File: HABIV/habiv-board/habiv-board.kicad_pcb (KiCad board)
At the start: 4 copper layers, 100.3 x 120.9 mm, 128 parts, among them IC1 RTC_PCF8523T, J1 Micro_SD_Card_Det, J10 Conn_01x02_Female, J11 Conn_01x02_Female, J12 Conn_01x02_Female, J13 Conn_01x02_Female, J14 Conn_01x02_Female, J15 Conn_01x02_Female, J16 Conn_01x02_Female, J17 Conn_01x03_Male, J18 Conn_01x03_Male, J19 Conn_01x03_Male, J2 Conn_ARM_JTAG_SWD_20, J20 Conn_01x05_Male, J21 Conn_01x04_Male, J3 Conn_01x02_Male, J4 Conn_01x16_Male, J5 Conn_01x03_Male, J6 Conn_01x16_Male, J7 Conn_01x16_Male, J8 Conn_01x02_Female, J9 Conn_01x02_Male, Q1 32.768KHz, SW1 SW_DPST_x2, U1 STM32F401RET6, U2 MAX31855, U3 FGPMMOPA6H, U4 TPS564208, U5 TPS564208, U6 LSM9DS1TR, U7 MS560702BA03-00, Y1 32.768MHz

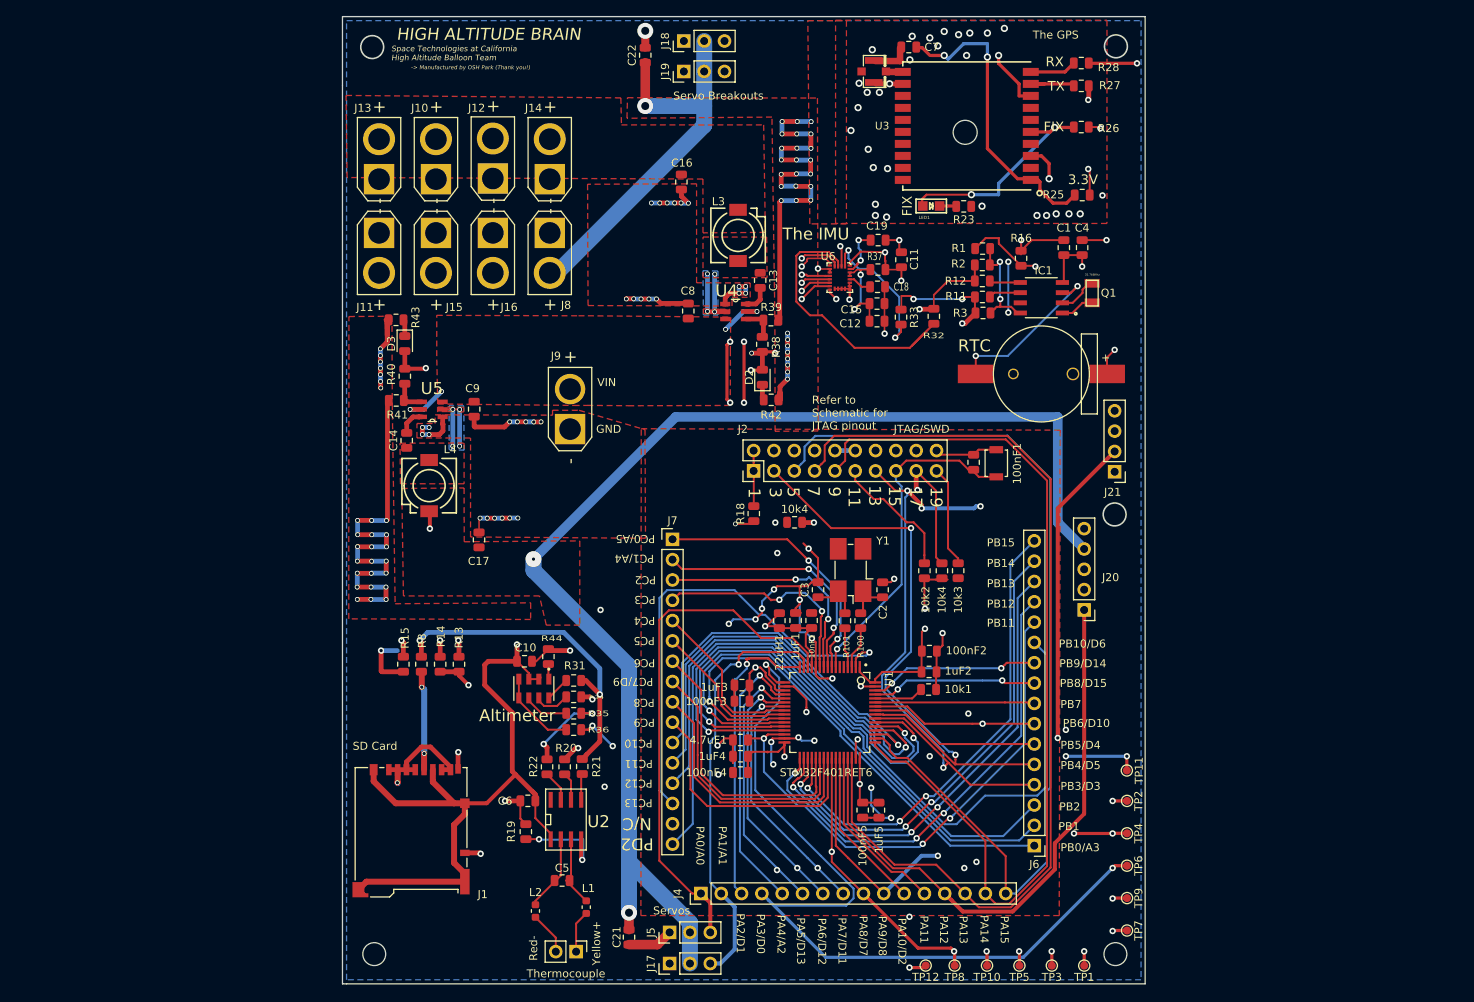
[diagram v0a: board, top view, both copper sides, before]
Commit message: Turned IMU into breakout pins, minor changes, unfinished!
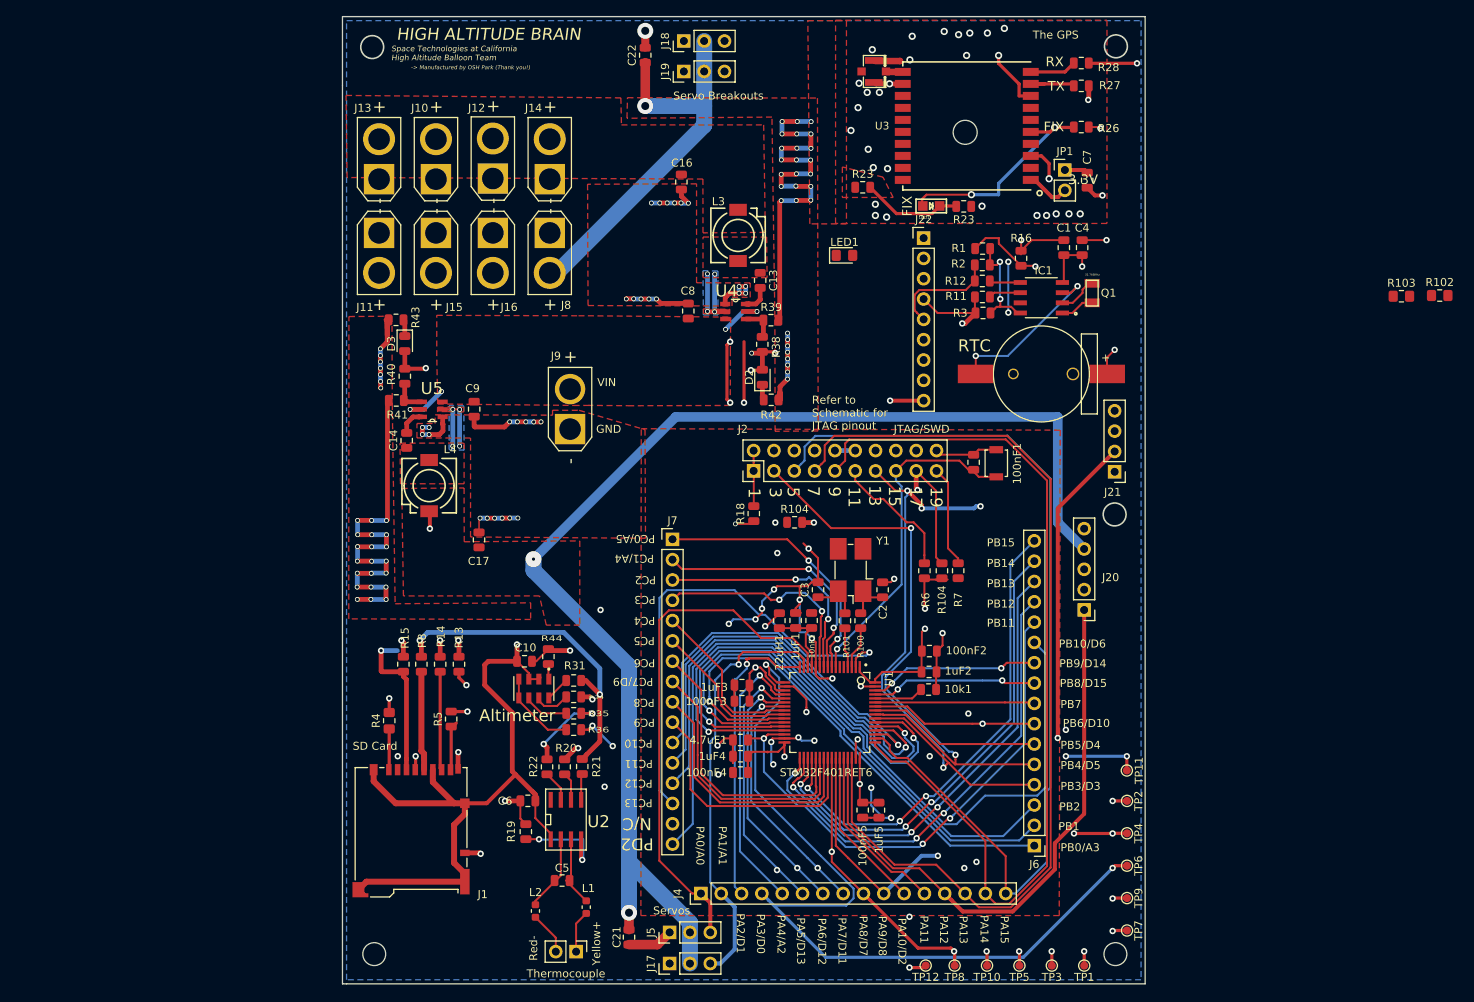
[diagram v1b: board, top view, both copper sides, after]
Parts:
- removed C11, C12, C19: 100n, Capacitor_SMD:C_0805_2012Metric
- removed C15: 10u, Capacitor_SMD:C_0805_2012Metric
- removed C18: 10n, Capacitor_SMD:C_0805_2012Metric
- removed R25, R32, R33, R37: 0, Resistor_SMD:R_0805_2012Metric
- removed U6: LSM9DS1TR, digikey-footprints:LGA-24_3x3.5mm_LSM9DS1
- added J22: Conn_01x09_Male, Connector_PinHeader_2.54mm:PinHeader_1x09_P2.54mm_Vertical, F.Cu at (153.7, 36.8)
- added JP1: Jumper, Connector_PinHeader_2.54mm:PinHeader_1x02_P2.54mm_Vertical, F.Cu at (171.3, 28.3)
- added LED1: RED, LED_SMD:LED_0805_2012Metric_Pad1.15x1.40mm_HandSolder, F.Cu at (143.8, 39.0)
- added R102: 10K, Resistor_SMD:R_0805_2012Metric_Pad1.15x1.40mm_HandSolder, F.Cu at (218.2, 44.0)
- added R103: 10K, Resistor_SMD:R_0805_2012Metric_Pad1.15x1.40mm_HandSolder, F.Cu at (213.4, 44.1)
- added R23: 1K, Resistor_SMD:R_0805_2012Metric, F.Cu at (146.1, 30.5)
- added R4: 0, Resistor_SMD:R_0805_2012Metric_Pad1.15x1.40mm_HandSolder, F.Cu at (86.9, 97.2)
- added R5: 0, Resistor_SMD:R_0805_2012Metric, F.Cu at (94.6, 96.9)
- R104 (x2): renamed from 10k4; value R8 -> 10K
- R6: renamed from 10k2; value R6 -> 10K
- R7: renamed from 10k3; value R7 -> 10K
- moved C7 27.8 mm to (174.1, 29.6), turned to 270 degrees
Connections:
- 10nF1 pad 2: +3V3 -> Net-(10nF1-Pad2)
- 1uF1 pad 2: +3V3 -> Net-(10nF1-Pad2)
- 22uH1 pad 1: +3V3 -> Net-(10nF1-Pad2)
- C7 pad 1: Net-(C7-Pad1) -> +3V3
- IC1 pad 7: (no net) -> Net-(IC1-Pad7)
- J1 pad 1: +3V3 -> Net-(J1-Pad1)
- J1 pad 2: +3V3 -> Net-(J1-Pad2)
- J1 pad 3: +3V3 -> Net-(J1-Pad3)
- J1 pad 7: +3V3 -> Net-(J1-Pad7)
- J1 pad 8: +3V3 -> Net-(J1-Pad8)
- J7 pad 15: (no net) -> Net-(J7-Pad15)
- R13 pad 2: +3V3 -> Net-(J1-Pad2)
- R14 pad 1: +3V3 -> Net-(J1-Pad7)
- R15 pad 2: +3V3 -> Net-(J1-Pad3)
- U1 pad 13: +3V3 -> Net-(10nF1-Pad2)
- U1 pad 5: (no net) -> Net-(U1-Pad5)
- U1 pad 6: (no net) -> Net-(U1-Pad6)
- U3 pad P$1: Net-(C7-Pad1) -> Net-(JP1-Pad2)
- U4 pad 5: Net-(C8-Pad1) -> Net-(R102-Pad1)
- U5 pad 5: Net-(C8-Pad1) -> Net-(R103-Pad1)
- Y1 pad 2: (no net) -> Net-(Y1-Pad2)
- Y1 pad 3: (no net) -> Net-(Y1-Pad3)
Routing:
- net PC3: track 82.1 -> 151.7 mm
- net +3V3: track 133.9 -> 81.8 mm, vias 21 -> 15
- net Net-(C7-Pad1): track 38.3 -> 0.00 mm, vias 2 -> 0
- net Net-(R32-Pad1): track 37.8 -> 0.00 mm
- net Net-(J1-Pad3): track 0.00 -> 19.8 mm, vias 0 -> 1
- net Net-(R33-Pad1): track 19.1 -> 0.00 mm, vias 2 -> 0
- net PC4: track 75.0 -> 59.7 mm, vias 3 -> 1
- net Net-(J1-Pad2): track 0.00 -> 14.6 mm, vias 0 -> 2
- net GND: track 424.3 -> 410.0 mm, vias 147 -> 142
- net Net-(C12-Pad1): track 12.9 -> 0.00 mm, vias 2 -> 0
- net Net-(C8-Pad1): track 12.7 -> 0.00 mm, vias 4 -> 0
- net Net-(J1-Pad7): track 0.00 -> 12.3 mm
- net PC2: track 76.6 -> 65.2 mm, vias 3 -> 2
- net PC6: track 94.4 -> 83.8 mm, vias 1 -> 0
- net Net-(LED1-PadC): track 2.08 -> 12.5 mm
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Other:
- net class Default: trace_width 0.4 -> 0.5
- board text removed: "The IMU"

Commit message: Changed IMU pinout, fixed some grounding issues
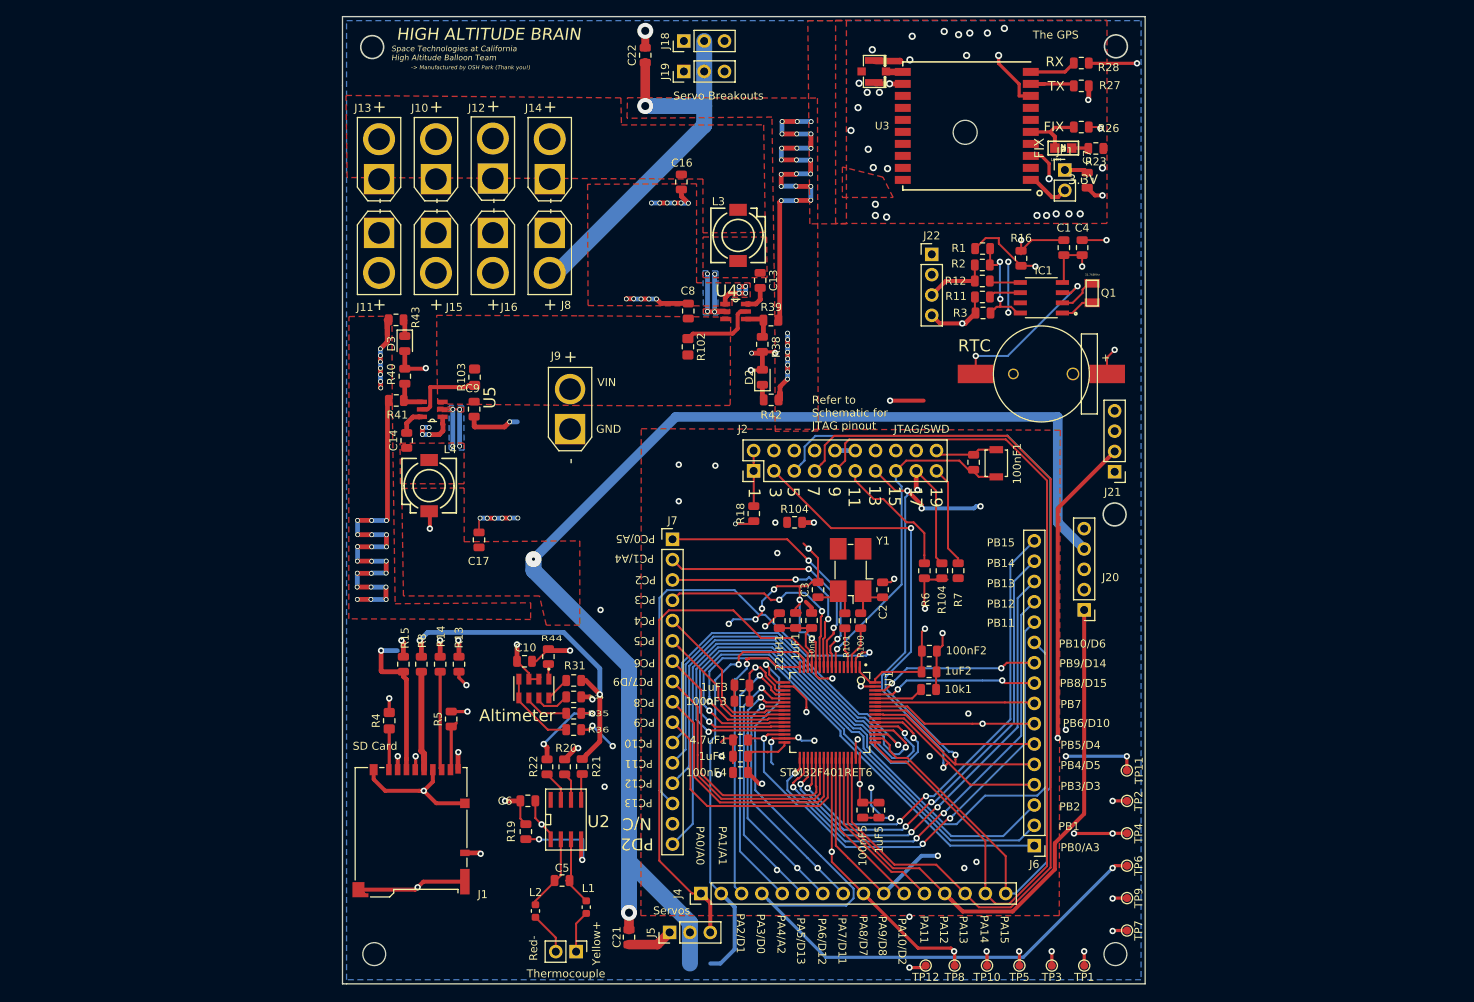
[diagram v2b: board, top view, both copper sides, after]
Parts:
- removed J17: Conn_01x03_Male, Connector_PinHeader_2.54mm:PinHeader_1x03_P2.54mm_Vertical
- removed the LED1 at (143.8, 39.0)
- removed the R23 at (146.1, 30.5)
- J22: value Conn_01x09_Male -> Conn_01x04_Male; footprint Connector_PinHeader_2.54mm:PinHeader_1x09_P2.54mm_Vertical -> Connector_PinHeader_2.54mm:PinHeader_1x04_P2.54mm_Vertical
- moved R103 116.3 mm to (97.5, 54.2), turned to 90 degrees
- moved R102 94.2 mm to (124.2, 50.4), turned to 270 degrees
- moved R23 18.0 mm to (175.2, 25.6)
- moved LED1 18.0 mm to (171.1, 25.6)
- moved J22 2.27 mm to (154.7, 38.9)
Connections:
- J22 pad 1: +3V3 -> GND
- J22 pad 2: Net-(J22-Pad2) -> +3V3
- J22 pad 3: GND -> PB9
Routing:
- net GND: track 410.0 -> 363.8 mm, vias 142 -> 143
- net PC4: track 59.7 -> 21.1 mm, vias 1 -> 0
- net Net-(LED1-PadA): track 27.9 -> 7.90 mm, vias 2 -> 0
- net Net-(LED1-PadC): track 12.5 -> 2.08 mm
- net PB9: track 109.7 -> 103.6 mm
- net Net-(R102-Pad1): track 6.33 -> 9.70 mm, vias 2 -> 0
- net PB8: track 121.7 -> 118.7 mm
- net Net-(R103-Pad1): track 6.33 -> 9.25 mm, vias 2 -> 0
- net Net-(J1-Pad2): track 14.6 -> 16.3 mm
- net PC7: track 125.3 -> 126.2 mm
- net +3V3: track 81.8 -> 82.4 mm
- net PC3: track 151.7 -> 151.3 mm, vias 5 -> 3

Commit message: Moved RockBlock Connector, removed some Servo breakouts
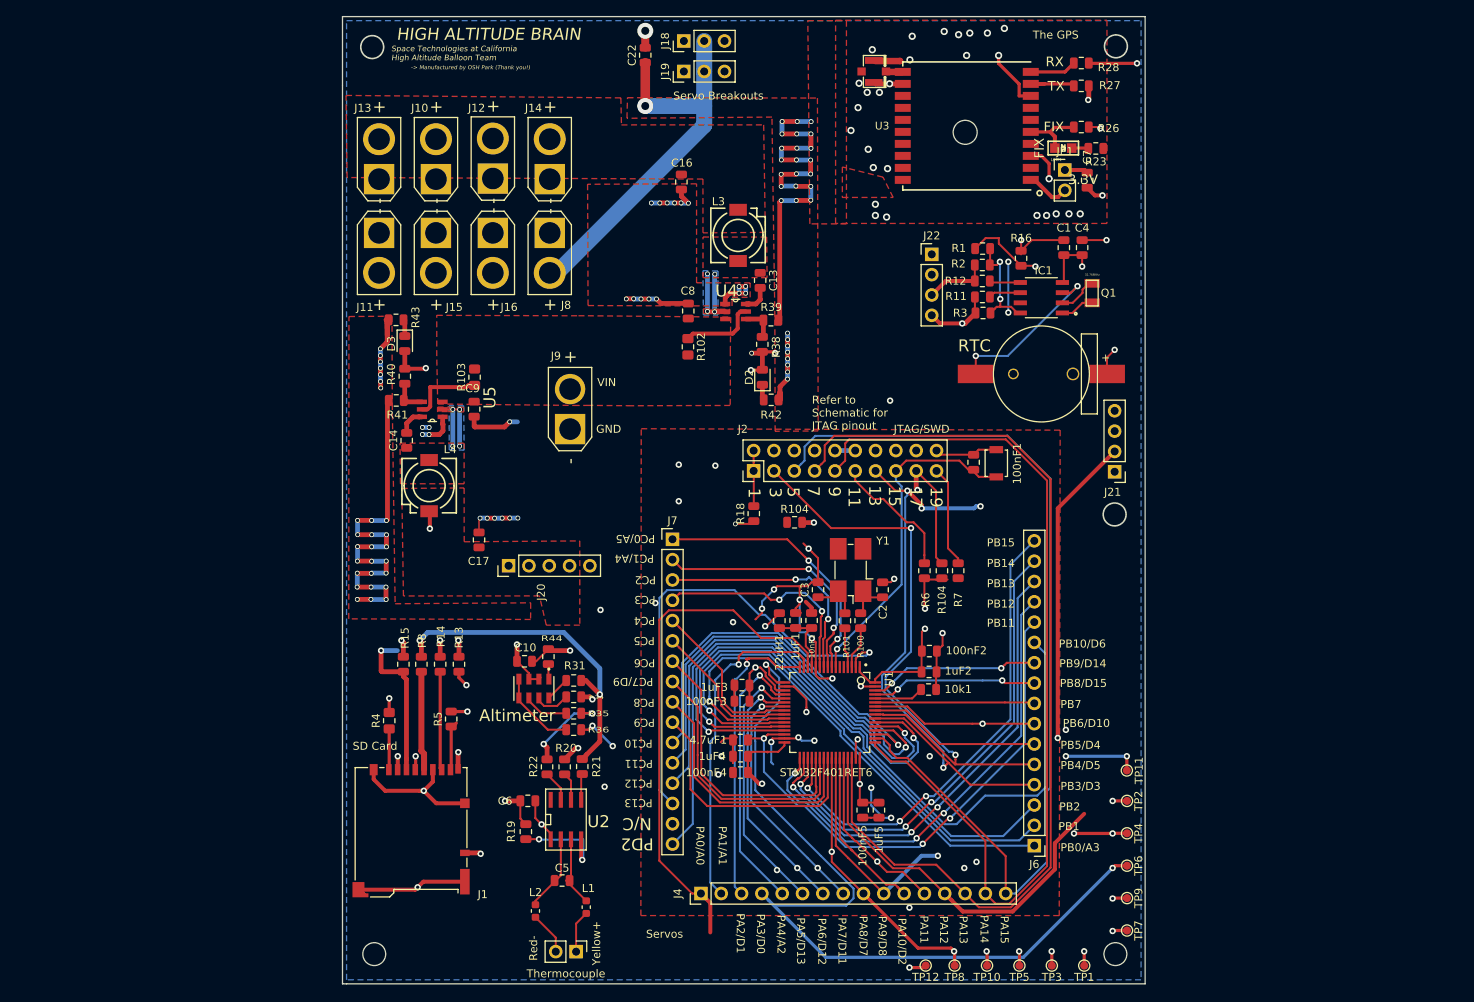
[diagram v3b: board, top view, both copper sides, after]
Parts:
- removed C21: 10u, Capacitor_SMD:C_0805_2012Metric
- removed J5: Conn_01x03_Male, Connector_PinHeader_2.54mm:PinHeader_1x03_P2.54mm_Vertical
- moved J20 72.2 mm to (101.8, 77.8), turned to 90 degrees
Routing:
- net +5V: track 296.7 -> 115.3 mm, vias 5 -> 3
- net PC8: track 90.4 -> 33.2 mm, vias 2 -> 0
- net PA12: track 74.8 -> 131.8 mm
- net PC5: track 75.4 -> 19.1 mm
- net PC6: track 83.8 -> 35.5 mm
- net PC3: track 151.3 -> 112.1 mm
- net PC2: track 65.2 -> 29.8 mm
- net PB10: track 105.3 -> 132.6 mm, vias 1 -> 2
- net GND: track 363.8 -> 342.2 mm, vias 143 -> 141
- net PA11: track 69.7 -> 84.4 mm
- net PA1: track 53.4 -> 42.0 mm
- net PA10: track 142.8 -> 144.8 mm
- net RST: track 88.0 -> 88.7 mm

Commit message: Added jumpers+ Rerouting
Added Jumpers to schematic. Rerouted trace PB10 from J20 as it was generating a design rules error. Also placed  some jumpers on board.
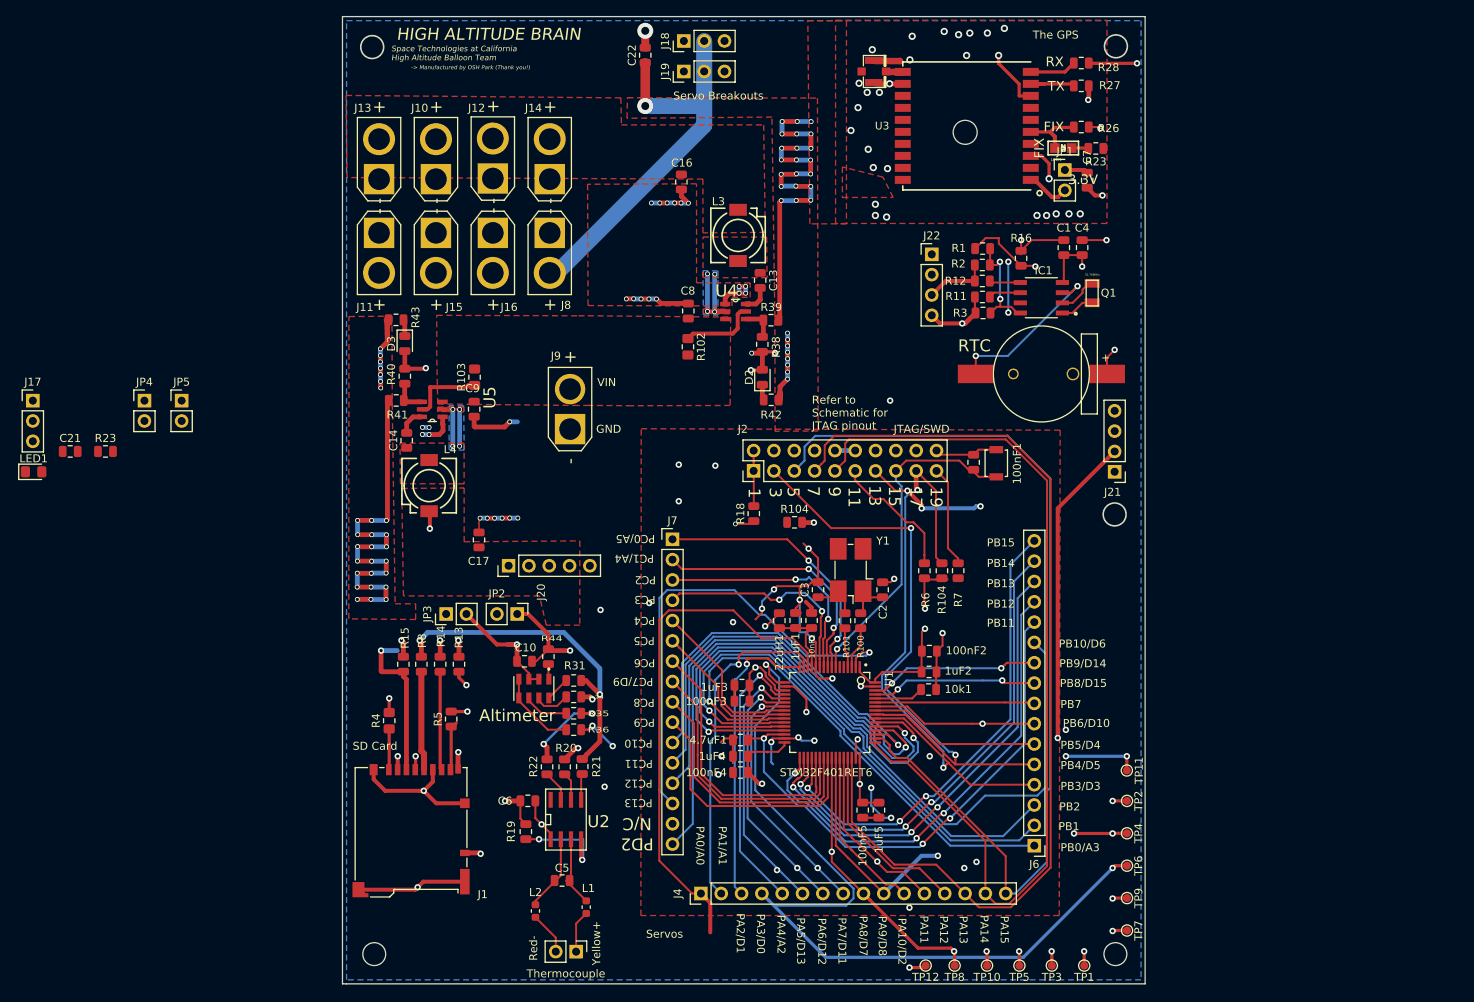
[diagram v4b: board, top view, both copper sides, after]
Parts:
- added C21: 10u, Capacitor_SMD:C_0805_2012Metric, F.Cu at (47.0, 63.5)
- added J17: Conn_01x03_Male, Connector_PinHeader_2.54mm:PinHeader_1x03_P2.54mm_Vertical, F.Cu at (42.3, 57.1)
- added JP2: Jumper, Connector_PinHeader_2.54mm:PinHeader_1x02_P2.54mm_Vertical, F.Cu at (102.9, 83.8)
- added JP3: Jumper, Connector_PinHeader_2.54mm:PinHeader_1x02_P2.54mm_Vertical, F.Cu at (94.0, 83.8)
- added JP4: Jumper, Connector_PinHeader_2.54mm:PinHeader_1x02_P2.54mm_Vertical, F.Cu at (56.3, 57.1)
- added JP5: Jumper, Connector_PinHeader_2.54mm:PinHeader_1x02_P2.54mm_Vertical, F.Cu at (60.9, 57.1)
- added LED1: RED, LED_SMD:LED_0805_2012Metric_Pad1.15x1.40mm_HandSolder, F.Cu at (42.4, 66.0)
- added R23: 1K, Resistor_SMD:R_0805_2012Metric, F.Cu at (51.4, 63.5)
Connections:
- C10 pad 1: +3V3 -> Net-(C10-Pad1)
- C10 pad 2: GND -> Net-(C10-Pad2)
- C6 pad 1: +3V3 -> Net-(C6-Pad1)
- C6 pad 2: GND -> Net-(C6-Pad2)
- R19 pad 1: +3V3 -> Net-(C6-Pad1)
- R44 pad 1: +3V3 -> Net-(C10-Pad1)
- U2 pad 1: GND -> Net-(C6-Pad2)
- U7 pad 2: GND -> Net-(C10-Pad2)
- U7 pad 3: GND -> Net-(C10-Pad2)
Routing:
- net PA12: track 131.8 -> 106.4 mm
- net Net-(C10-Pad2): track 0.00 -> 15.6 mm, vias 0 -> 1
- net Net-(C10-Pad1): track 0.00 -> 12.3 mm, vias 0 -> 1
- net GND: track 342.2 -> 330.1 mm, vias 141 -> 139
- net +3V3: track 82.4 -> 71.8 mm, vias 15 -> 13
- net Net-(C6-Pad2): track 0.00 -> 5.60 mm, vias 0 -> 1
- net Net-(C6-Pad1): track 0.00 -> 5.12 mm, vias 0 -> 1
